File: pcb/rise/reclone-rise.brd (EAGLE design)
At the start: 100 x 80 mm, 0 parts

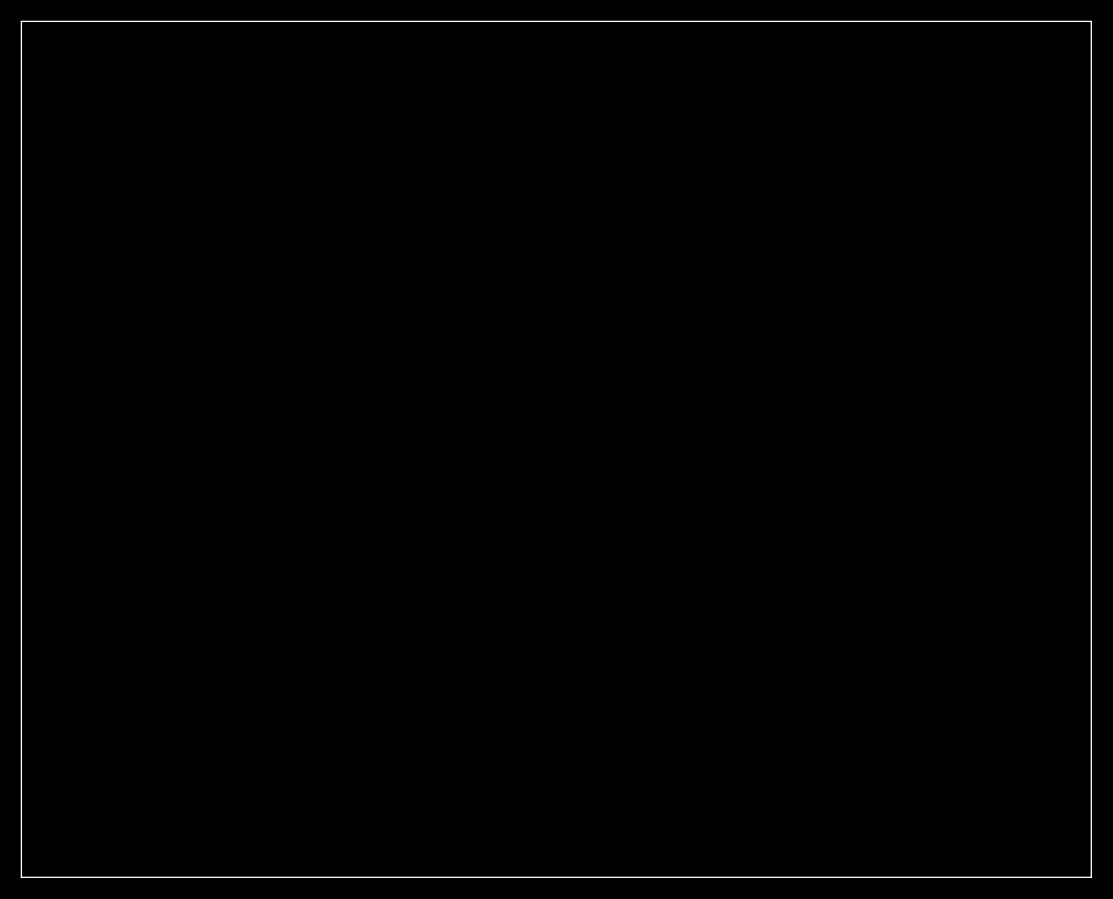
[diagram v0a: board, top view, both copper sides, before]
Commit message: Added board dimensions, holes, and a couple parts for microcontroller and FPGA
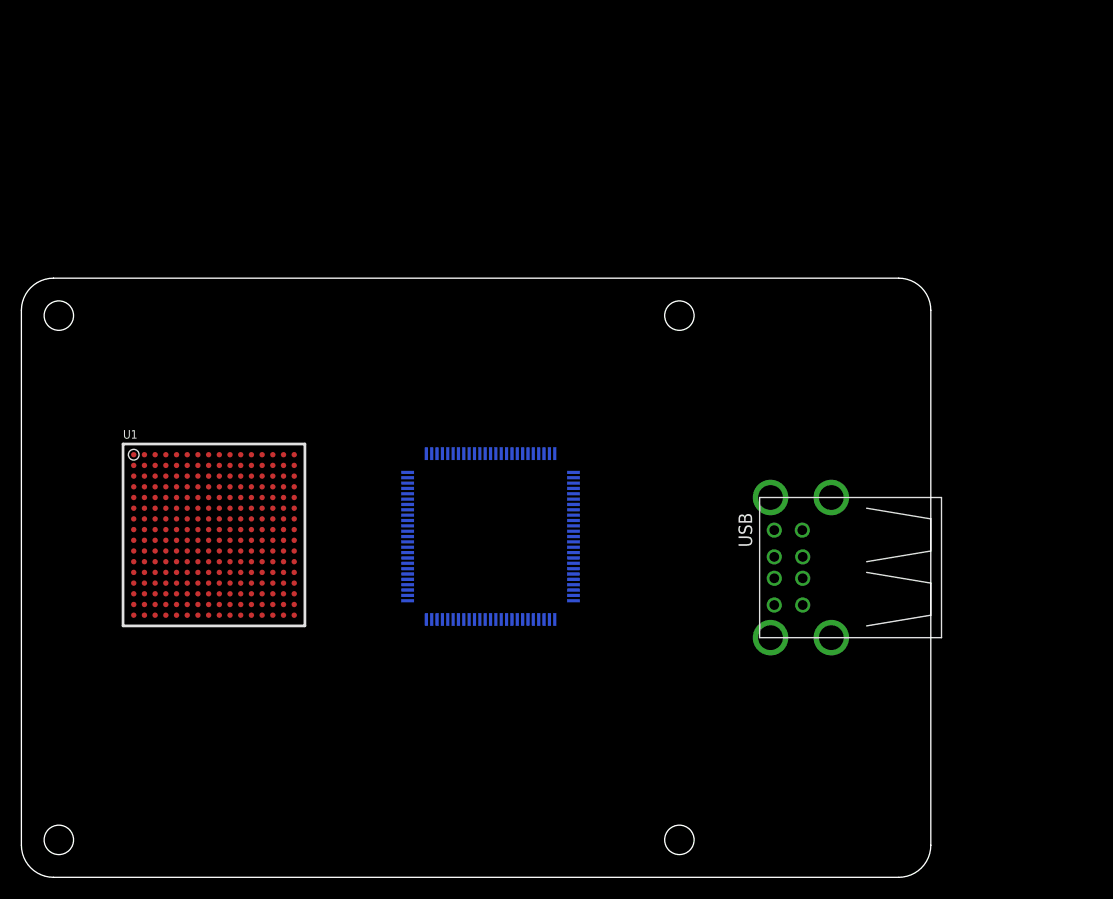
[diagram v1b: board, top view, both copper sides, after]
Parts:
- added MCU: STM32F407VGT6, reclone-rise:LQFP-100
- added U1: 6SLX25FTG256, xilinx_devices_V6:FT256
- added USB: USB_A_2H, reclone-rise:USB-A-2H
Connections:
- new net GND: U1.A1, U1.A16, U1.B11, U1.B7, U1.D13, U1.D4, U1.E9, U1.G15, U1.G2, U1.G8, U1.H12, U1.H7, U1.H9, U1.J5, U1.J8, U1.K7, U1.K9, U1.L15, U1.L2, U1.M8, U1.N13, U1.P3, U1.R10, U1.R6, U1.T1, U1.T16
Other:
- board size 100 x 80 mm -> 85 x 56 mm

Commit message: Added a ton of components just to get a sense for whether layout is possible on the top of the board
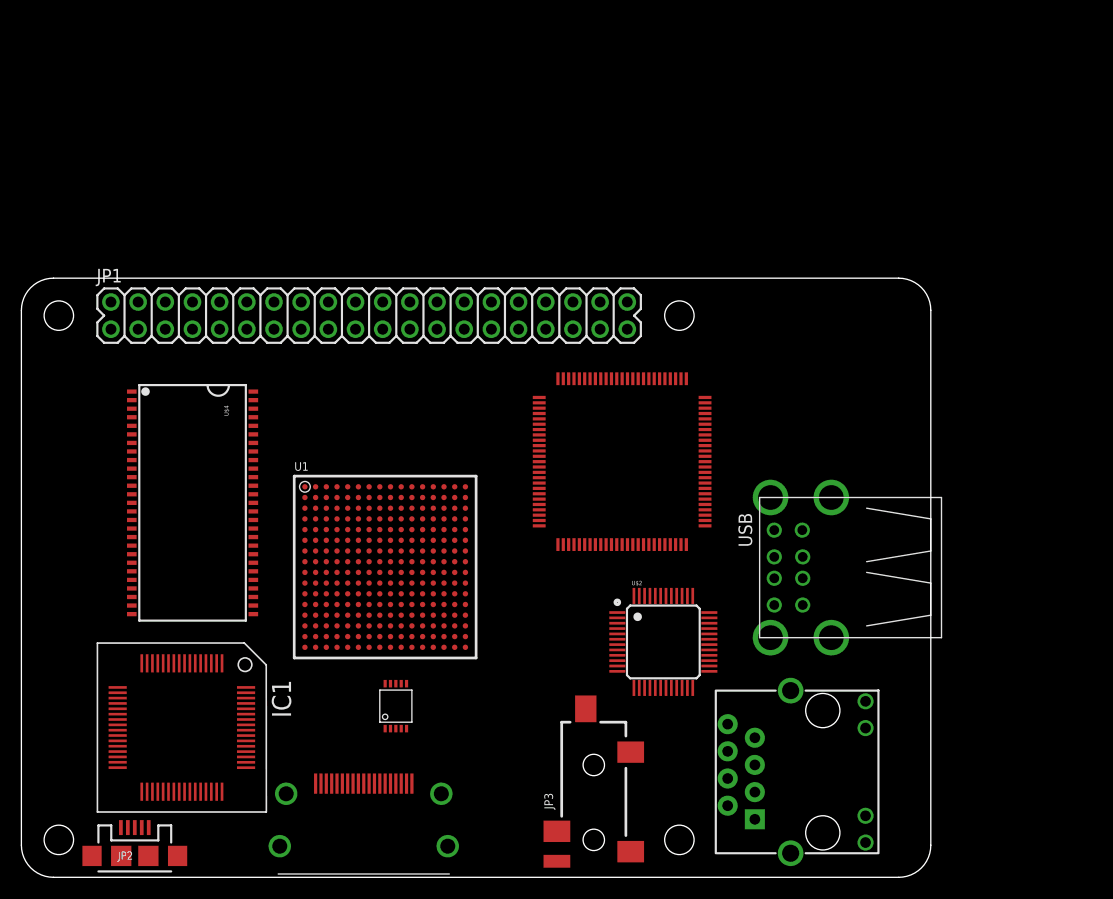
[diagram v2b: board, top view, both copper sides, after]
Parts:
- added IC1: (no value), ftdichip-3:TQFP64-12X12
- added J1: MAGJACK, SparkFun-Connectors:MAGJACK
- added JP1: M20X2, SparkFun-Connectors:2X20
- added JP2: USB-MICROB, SparkFun-Connectors:USB-MICROB
- added JP3: (no value), SparkFun-Connectors:AUDIO-JACK-3.5MM-SMD
- added U$1: PCA9527, reclone-rise:TSSOP10
- added U$2: DP83848C, reclone-rise:LQFP-48
- added U$3: HDMI_A, reclone-rise:HDMI_A_SMT
- added U$4: MT48LC16M16A2P, reclone-rise:TSOP54-400
- moved U1 16.3 mm to (34.0, 29.0)
- moved MCU 7.28 mm to (49.0, 46.0), flipped to the top
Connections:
- new net AGND: IC1.10
- new net VCCIO: IC1.20, IC1.31, IC1.42, IC1.56
- new net VCORE: IC1.12, IC1.37, IC1.64
- new net VPHY: IC1.4
- new net VPLL: IC1.9
- net GND: now also IC1.1, IC1.11, IC1.15, IC1.25, IC1.35, IC1.47, IC1.5, IC1.51
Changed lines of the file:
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@@
 <elements>
 <element name="USB" library="reclone-rise" package="USB-A-2H" value="USB_A_2H" x="69" y="29" rot="R180"/>
-<element name="MCU" library="reclone-rise" package="LQFP-100" value="STM32F407VGT6" x="51" y="39" rot="MR270"/>
-<element name="U1" library="xilinx_devices_V6" package="FT256" value="6SLX25FTG256" x="18" y="32"/>
+<element name="MCU" library="reclone-rise" package="LQFP-100" value="STM32F407VGT6" x="49" y="46" rot="R270"/>
+<element name="U1" library="xilinx_devices_V6" package="FT256" value="6SLX25FTG256" x="34" y="29"/>
+<element name="JP1" library="SparkFun-Connectors" package="2X20" value="M20X2" x="32.5" y="52.5"/>
+<element name="J1" library="SparkFun-Connectors" package="MAGJACK" value="MAGJACK" x="86" y="2.25" rot="R90"/>
+<element name="IC1" library="ftdichip-3" package="TQFP64-12X12" value="" x="15" y="14" rot="R180"/>
+<element name="JP2" library="SparkFun-Connectors" package="USB-MICROB" value="USB-MICROB" x="10.6" y="2">
+<attribute name="PROD_ID" value="CONN-09505" x="10.6" y="2" size="1.778" layer="27" display="off"/>
+</element>
+<element name="JP3" library="SparkFun-Connectors" package="AUDIO-JACK-3.5MM-SMD" value="" x="53.5" y="0" rot="R90">
+<attribute name="PROD_ID" value="CONN-10353" x="53.5" y="0" size="1.778" layer="27" rot="R90" display="off"/>
+</element>
+<element name="U$1" library="reclone-rise" package="TSSOP10" value="PCA9527" x="35" y="16" rot="R90"/>
+<element name="U$2" library="reclone-rise" package="LQFP-48" value="DP83848C" x="60" y="22"/>
+<element name="U$3" library="reclone-rise" package="HDMI_A_SMT" value="HDMI_A" x="32" y="4" rot="R270"/>
+<element name="U$4" library="reclone-rise" package="TSOP54-400" value="MT48LC16M16A2P" x="16" y="35" rot="R270"/>
 </elements>
 <signals>
@@
 <contactref element="U1" pad="T1"/>
 <contactref element="U1" pad="T16"/>
-<wire x1="22.5" y1="36.5" x2="25.5" y2="39.5" width="0" layer="19" extent="1-1"/>
-<wire x1="20.5" y1="38.5" x2="22.5" y2="36.5" width="0" layer="19" extent="1-1"/>
-<wire x1="24.5" y1="33.5" x2="22.5" y2="36.5" width="0" layer="19" extent="1-1"/>
-<wire x1="21.5" y1="32.5" x2="24.5" y2="33.5" width="0" layer="19" extent="1-1"/>
-<wire x1="18.5" y1="32.5" x2="21.5" y2="32.5" width="0" layer="19" extent="1-1"/>
-<wire x1="17.5" y1="33.5" x2="18.5" y2="32.5" width="0" layer="19" extent="1-1"/>
-<wire x1="16.5" y1="32.5" x2="17.5" y2="33.5" width="0" layer="19" extent="1-1"/>
-<wire x1="17.5" y1="31.5" x2="18.5" y2="32.5" width="0" layer="19" extent="1-1"/>
-<wire x1="18.5" y1="30.5" x2="17.5" y2="31.5" width="0" layer="19" extent="1-1"/>
-<wire x1="16.5" y1="30.5" x2="17.5" y2="31.5" width="0" layer="19" extent="1-1"/>
-<wire x1="18.5" y1="35.5" x2="17.5" y2="33.5" width="0" layer="19" extent="1-1"/>
-<wire x1="14.5" y1="31.5" x2="16.5" y2="32.5" width="0" layer="19" extent="1-1"/>
-<wire x1="17.5" y1="28.5" x2="18.5" y2="30.5" width="0" layer="19" extent="1-1"/>
-<wire x1="16.5" y1="38.5" x2="18.5" y2="35.5" width="0" layer="19" extent="1-1"/>
-<wire x1="13.5" y1="36.5" x2="16.5" y2="38.5" width="0" layer="19" extent="1-1"/>
-<wire x1="11.5" y1="33.5" x2="14.5" y2="31.5" width="0" layer="19" extent="1-1"/>
-<wire x1="19.5" y1="25.5" x2="17.5" y2="28.5" width="0" layer="19" extent="1-1"/>
-<wire x1="22.5" y1="27.5" x2="19.5" y2="25.5" width="0" layer="19" extent="1-1"/>
-<wire x1="24.5" y1="29.5" x2="22.5" y2="27.5" width="0" layer="19" extent="1-1"/>
-<wire x1="15.5" y1="25.5" x2="17.5" y2="28.5" width="0" layer="19" extent="1-1"/>
-<wire x1="12.5" y1="26.5" x2="15.5" y2="25.5" width="0" layer="19" extent="1-1"/>
-<wire x1="10.5" y1="24.5" x2="12.5" y2="26.5" width="0" layer="19" extent="1-1"/>
-<wire x1="11.5" y1="29.5" x2="12.5" y2="26.5" width="0" layer="19" extent="1-1"/>
-<wire x1="10.5" y1="39.5" x2="13.5" y2="36.5" width="0" layer="19" extent="1-1"/>
-<wire x1="25.5" y1="24.5" x2="22.5" y2="27.5" width="0" layer="19" extent="1-1"/>
+<contactref element="IC1" pad="1"/>
+<contactref element="IC1" pad="5"/>
+<contactref element="IC1" pad="11"/>
+<contactref element="IC1" pad="15"/>
+<contactref element="IC1" pad="25"/>
+<contactref element="IC1" pad="35"/>
+<contactref element="IC1" pad="47"/>
+<contactref element="IC1" pad="51"/>
+<wire x1="38.5" y1="33.5" x2="41.5" y2="36.5" width="0" layer="19" extent="1-1"/>
+<wire x1="36.5" y1="35.5" x2="38.5" y2="33.5" width="0" layer="19" extent="1-1"/>
+<wire x1="40.5" y1="30.5" x2="38.5" y2="33.5" width="0" layer="19" extent="1-1"/>
+<wire x1="37.5" y1="29.5" x2="40.5" y2="30.5" width="0" layer="19" extent="1-1"/>
+<wire x1="34.5" y1="29.5" x2="37.5" y2="29.5" width="0" layer="19" extent="1-1"/>
+<wire x1="33.5" y1="30.5" x2="34.5" y2="29.5" width="0" layer="19" extent="1-1"/>
+<wire x1="32.5" y1="29.5" x2="33.5" y2="30.5" width="0" layer="19" extent="1-1"/>
+<wire x1="33.5" y1="28.5" x2="34.5" y2="29.5" width="0" layer="19" extent="1-1"/>
+<wire x1="34.5" y1="27.5" x2="33.5" y2="28.5" width="0" layer="19" extent="1-1"/>
+<wire x1="32.5" y1="27.5" x2="33.5" y2="28.5" width="0" layer="19" extent="1-1"/>
+<wire x1="34.5" y1="32.5" x2="33.5" y2="30.5" width="0" layer="19" extent="1-1"/>
+<wire x1="30.5" y1="28.5" x2="32.5" y2="29.5" width="0" layer="19" extent="1-1"/>
+<wire x1="33.5" y1="25.5" x2="34.5" y2="27.5" width="0" layer="19" extent="1-1"/>
+<wire x1="32.5" y1="35.5" x2="34.5" y2="32.5" width="0" layer="19" extent="1-1"/>
+<wire x1="29.5" y1="33.5" x2="32.5" y2="35.5" width="0" layer="19" extent="1-1"/>
+<wire x1="27.5" y1="30.5" x2="30.5" y2="28.5" width="0" layer="19" extent="1-1"/>
+<wire x1="35.5" y1="22.5" x2="33.5" y2="25.5" width="0" layer="19" extent="1-1"/>
+<wire x1="38.5" y1="24.5" x2="35.5" y2="22.5" width="0" layer="19" extent="1-1"/>
+<wire x1="40.5" y1="26.5" x2="38.5" y2="24.5" width="0" layer="19" extent="1-1"/>
+<wire x1="31.5" y1="22.5" x2="33.5" y2="25.5" width="0" layer="19" extent="1-1"/>
+<wire x1="28.5" y1="23.5" x2="31.5" y2="22.5" width="0" layer="19" extent="1-1"/>
+<wire x1="26.5" y1="21.5" x2="28.5" y2="23.5" width="0" layer="19" extent="1-1"/>
+<wire x1="27.5" y1="26.5" x2="28.5" y2="23.5" width="0" layer="19" extent="1-1"/>
+<wire x1="26.5" y1="36.5" x2="29.5" y2="33.5" width="0" layer="19" extent="1-1"/>
+<wire x1="41.5" y1="21.5" x2="38.5" y2="24.5" width="0" layer="19" extent="1-1"/>
+<wire x1="18.2501" y1="7.9999" x2="26.5" y2="21.5" width="0" layer="19" extent="1-1"/>
+<wire x1="21.0001" y1="11.25" x2="18.2501" y2="7.9999" width="0" layer="19" extent="1-1"/>
+<wire x1="12.2499" y1="7.9999" x2="18.2501" y2="7.9999" width="0" layer="19" extent="1-1"/>
+<wire x1="8.9999" y1="13.75" x2="12.2499" y2="7.9999" width="0" layer="19" extent="1-1"/>
+<wire x1="11.75" y1="20.0001" x2="8.9999" y2="13.75" width="0" layer="19" extent="1-1"/>
+<wire x1="13.75" y1="20.0001" x2="11.75" y2="20.0001" width="0" layer="19" extent="1-1"/>
+<wire x1="16.75" y1="20.0001" x2="13.75" y2="20.0001" width="0" layer="19" extent="1-1"/>
+<wire x1="18.75" y1="20.0001" x2="16.75" y2="20.0001" width="0" layer="19" extent="1-1"/>
+</signal>
+<signal name="AGND">
+<contactref element="IC1" pad="10"/>
+</signal>
+<signal name="VPHY">
+<contactref element="IC1" pad="4"/>
+</signal>
+<signal name="VCORE">
+<contactref element="IC1" pad="12"/>
+<contactref element="IC1" pad="37"/>
+<contactref element="IC1" pad="64"/>
+<wire x1="13.2501" y1="20.0001" x2="13.2499" y2="7.9999" width="0" layer="19" extent="1-1"/>
+<wire x1="21.0001" y1="17.7501" x2="13.2501" y2="20.0001" width="0" layer="19" extent="1-1"/>
+</signal>
+<signal name="VCCIO">
+<contactref element="IC1" pad="31"/>
+<contactref element="IC1" pad="20"/>
+<contactref element="IC1" pad="42"/>
+<contactref element="IC1" pad="56"/>
+<wire x1="8.9999" y1="16.2499" x2="8.9999" y2="10.7531" width="0" layer="19" extent="1-1"/>
+<wire x1="15.75" y1="7.9999" x2="8.9999" y2="10.7531" width="0" layer="19" extent="1-1"/>
+<wire x1="21.0001" y1="13.7499" x2="15.75" y2="7.9999" width="0" layer="19" extent="1-1"/>
+</signal>
+<signal name="VPLL">
+<contactref element="IC1" pad="9"/>
 </signal>
 </signals>
